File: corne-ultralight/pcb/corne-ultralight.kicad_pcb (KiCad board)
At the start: 2 copper layers, 275.5 x 105.6 mm, 136 parts, among them J2 OLED, J5 Breakaway_Tabs, J7 OLED, SW1 SW_PUSH, SW10 SW_PUSH, SW11 SW_PUSH, SW12 SW_PUSH, SW13 SW_PUSH, SW14 SW_PUSH, SW15 SW_PUSH, SW16 SW_PUSH, SW17 SW_PUSH, SW18 SW_PUSH, SW19 SW_PUSH, SW2 SW_PUSH, SW20 SW_PUSH, SW21 SW_PUSH, SW22 SW_PUSH, SW23 SW_PUSH, SW24 SW_PUSH, SW25 SW_PUSH, SW26 SW_PUSH, SW27 SW_PUSH, SW28 SW_PUSH, SW29 SW_PUSH, SW3 SW_PUSH, SW30 SW_PUSH, SW31 SW_PUSH, SW32 SW_PUSH, SW33 SW_PUSH, SW34 SW_PUSH, SW35 SW_PUSH, SW36 SW_PUSH, SW37 SW_PUSH, SW38 SW_PUSH, SW39 SW_PUSH, SW4 SW_PUSH, SW40 SW_PUSH, SW41 SW_PUSH, SW42 SW_PUSH, SW5 SW_PUSH, SW6 SW_PUSH, SW7 SW_PUSH, SW8 SW_PUSH, SW9 SW_PUSH, U1 ProMicro, U2 ProMicro

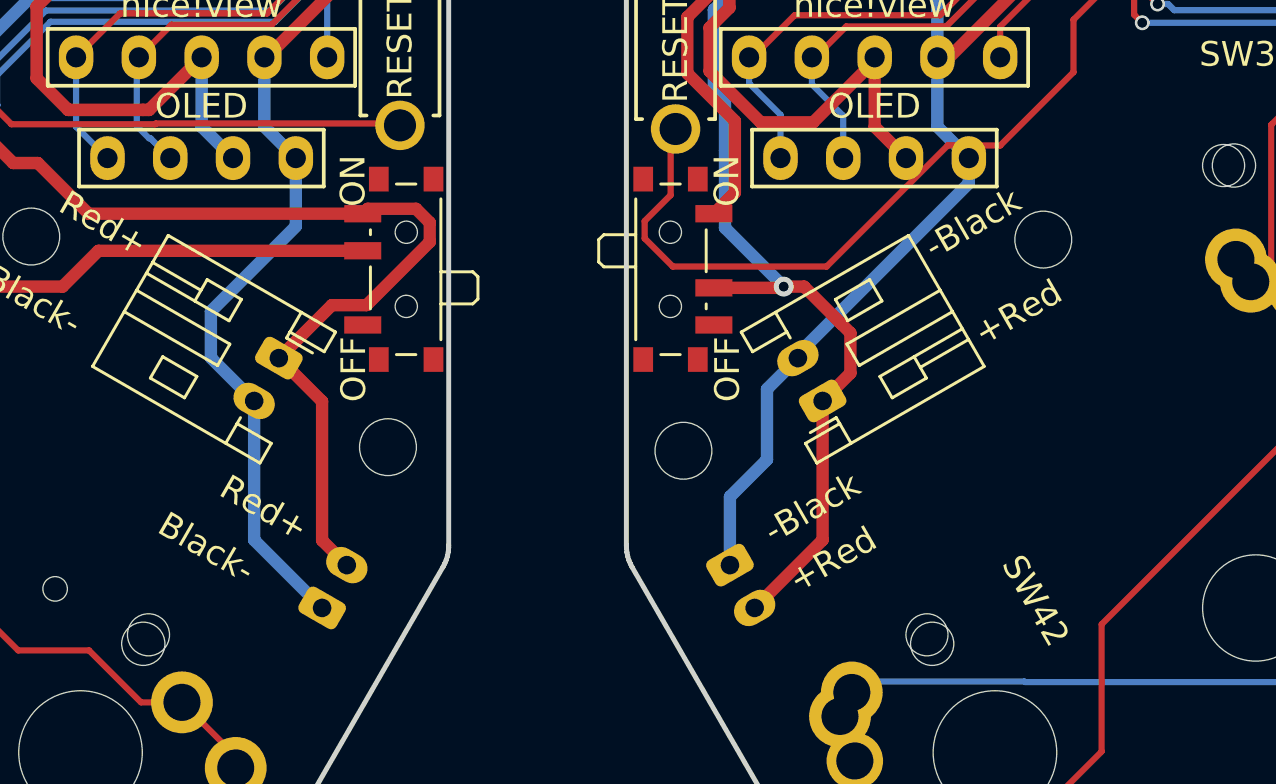
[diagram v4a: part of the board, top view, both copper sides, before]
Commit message: All JST connectors routed
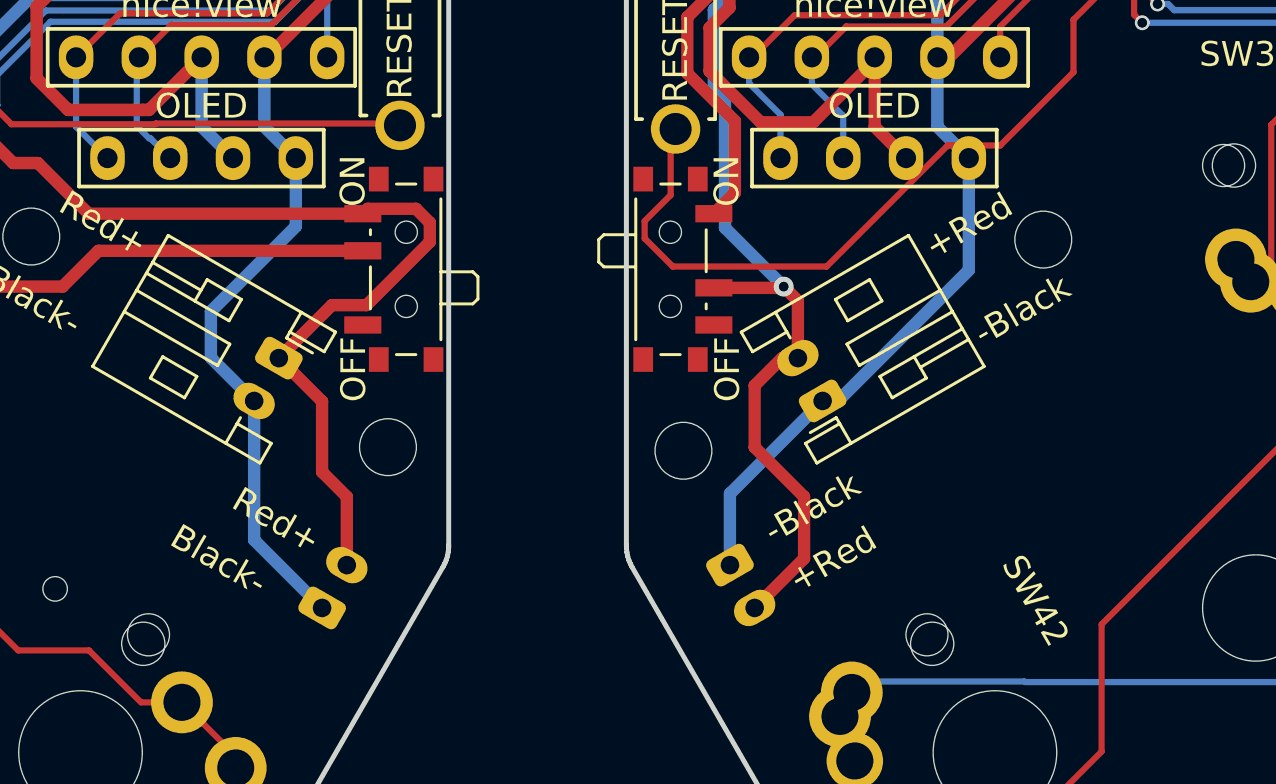
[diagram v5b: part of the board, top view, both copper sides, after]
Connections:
- BATJ5 pad 1: Net-(BATJ5-Pin_2) -> GNDA
- BATJ5 pad 2: GNDA -> Net-(BATJ5-Pin_2)
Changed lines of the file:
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@@
 			(remove_unused_layers no)
 			(roundrect_rratio 0.208333)
-			(net 18 "Net-(BATJ5-Pin_2)")
+			(net 38 "GNDA")
 			(pinfunction "Pin_1")
 			(pintype "passive")
@@
 			(layers "*.Cu" "*.Mask")
 			(remove_unused_layers no)
-			(net 38 "GNDA")
+			(net 18 "Net-(BATJ5-Pin_2)")
 			(pinfunction "Pin_2")
 			(pintype "passive")
@@
 	)
 	(gr_text "-Black"
-		(at 165.125347 79.445 90)
+		(at 166.7125 81.445 90)
 		(layer "B.SilkS")
 		(effects
@@
 	)
 	(gr_text "-Black"
-		(at 137.8625 79.445 90)
+		(at 138.2125 90.445 -30)
 		(layer "B.SilkS")
 		(effects
@@
 	)
 	(gr_text "-Black"
-		(locked yes)
-		(at 135.8375 95.945 -30)
+		(at 139.2125 80.945 90)
+		(layer "B.SilkS")
+		(effects
+			(font
+				(size 1 1)
+				(thickness 0.15)
+			)
+			(justify left mirror)
+		)
+	)
+	(gr_text "-Black"
+		(at 135.2125 96.945 -30)
 		(layer "B.SilkS")
 		(effects
@@
 	)
 	(gr_text "+Red"
-		(at 135.7375 79.445 90)
+		(at 134.2125 81.445 90)
+		(layer "B.SilkS")
+		(effects
+			(font
+				(size 1 1)
+				(thickness 0.15)
+			)
+			(justify left mirror)
+		)
+	)
+	(gr_text "Red+"
+		(at 165.7125 86.445 30)
 		(layer "B.SilkS")
 		(effects
@@
 	)
 	(gr_text "Black-"
-		(at 168.9625 91.195 30)
+		(at 168.2125 90.945 30)
 		(layer "B.SilkS")
 		(effects
@@
 	)
 	(gr_text "+Red"
-		(locked yes)
-		(at 136.7125 94.445 330)
+		(at 137.2125 93.945 330)
 		(layer "B.SilkS")
 		(effects
@@
 	)
 	(gr_text "+Red"
-		(at 163.000347 79.445 90)
+		(at 139.2125 88.445 330)
+		(layer "B.SilkS")
+		(effects
+			(font
+				(size 1 1)
+				(thickness 0.15)
+			)
+			(justify left mirror)
+		)
+	)
+	(gr_text "Black-"
+		(at 167.7125 87.945 30)
+		(layer "B.SilkS")
+		(effects
+			(font
+				(size 1 1)
+				(thickness 0.15)
+			)
+			(justify left mirror)
+		)
+	)
+	(gr_text "+Red"
+		(at 161.7125 81.445 90)
 		(layer "B.SilkS")
 		(effects
@@
 	)
 	(gr_text "Red+"
-		(at 168.9625 93.695 30)
+		(at 169.2125 94.445 30)
 		(layer "B.SilkS")
 		(effects
@@
 	)
 	(gr_text "-Black"
-		(at 166.2125 84.945 30)
+		(at 168.2125 88.445 30)
 		(layer "F.SilkS")
 		(effects
@@
 	)
 	(gr_text "Red+"
-		(at 137.7125 94.445 -30)
+		(at 138.2125 94.945 -30)
 		(layer "F.SilkS")
 		(effects
@@
 	)
 	(gr_text "+Red"
-		(at 168.2125 88.445 30)
+		(at 166.2125 84.945 30)
 		(layer "F.SilkS")
 		(effects
@@
 	)
 	(gr_text "Black-"
-		(at 135.2125 95.945 -30)
+		(at 135.7125 96.445 -30)
 		(layer "F.SilkS")
 		(effects
@@
 	)
 	(segment
+		(start 138.9625 91.07)
+		(end 138.9625 96.695)
+		(width 0.5)
+		(layer "B.Cu")
+		(net 5)
+	)
+	(segment
 		(start 139.3785 77.168)
 		(end 139.3785 79.975)
@@
 	)
 	(segment
+		(start 138.9625 96.695)
+		(end 141.7125 99.445)
+		(width 0.5)
+		(layer "B.Cu")
+		(net 5)
+	)
+	(segment
 		(start 127.5605 44.622)
 		(end 126.2625 45.92)
@@
 	)
 	(segment
-		(start 138.9625 96.695)
-		(end 141.7125 99.445)
-		(width 0.5)
-		(layer "B.Cu")
-		(net 5)
-	)
-	(segment
-		(start 138.9625 91.07)
-		(end 138.9625 96.695)
-		(width 0.5)
-		(layer "B.Cu")
-		(net 5)
-	)
-	(segment
 		(start 134.7115 79.295)
 		(end 136.8385 77.168)
@@
 	)
 	(segment
-		(start 141.7125 96.712949)
-		(end 142.7125 97.712949)
-		(width 0.5)
-		(layer "F.Cu")
-		(net 17)
-	)
-	(segment
 		(start 143.511003 87.195)
 		(end 142.105449 87.195)
@@
 	)
 	(segment
+		(start 141.7125 91.087949)
+		(end 141.7125 93.945)
+		(width 0.5)
+		(layer "F.Cu")
+		(net 17)
+	)
+	(segment
 		(start 146.0675 84.638503)
 		(end 143.511003 87.195)
@@
 	)
 	(segment
-		(start 141.7125 91.087949)
-		(end 141.7125 96.712949)
+		(start 145.511003 83.295)
+		(end 146.0675 83.851497)
 		(width 0.5)
 		(layer "F.Cu")
@@
 	)
 	(segment
-		(start 145.511003 83.295)
-		(end 146.0675 83.851497)
+		(start 143.5575 83.295)
+		(end 145.511003 83.295)
 		(width 0.5)
 		(layer "F.Cu")
@@
 	)
 	(segment
-		(start 143.5575 83.295)
-		(end 145.511003 83.295)
+		(start 141.7125 93.945)
+		(end 142.7125 94.945)
 		(width 0.5)
 		(layer "F.Cu")
@@
 	)
 	(segment
+		(start 142.7125 94.945)
+		(end 142.7125 97.712949)
+		(width 0.5)
+		(layer "F.Cu")
+		(net 17)
+	)
+	(segment
 		(start 143.3575 83.495)
 		(end 143.5575 83.295)
@@
 	)
 	(segment
-		(start 161.9625 96.695)
-		(end 161.9625 91.07)
+		(start 159.2125 90.445)
+		(end 159.2125 92.945)
 		(width 0.5)
 		(layer "F.Cu")
@@
 	)
 	(segment
-		(start 159.2125 99.445)
-		(end 161.9625 96.695)
+		(start 161.2125 97.445)
+		(end 161.2125 94.945)
 		(width 0.5)
 		(layer "F.Cu")
@@
 	)
 	(segment
-		(start 161.2125 86.445)
-		(end 162.7125 87.945)
+		(start 159.2125 92.945)
+		(end 161.2125 94.945)
 		(width 0.5)
 		(layer "F.Cu")
@@
 	)
 	(segment
-		(start 160.3875 86.445)
-		(end 161.2125 86.445)
+		(start 159.2125 99.445)
+		(end 161.2125 97.445)
+		(width 0.5)
+		(layer "F.Cu")
+		(net 18)
+	)
+	(segment
+		(start 160.9625 89.337949)
+		(end 160.319551 89.337949)
 		(width 0.5)
 		(layer "F.Cu")
@@
 	)
 	(segment
-		(start 163.0875 89.945)
-		(end 163.0875 88.32)
+		(start 160.9625 89.337949)
+		(end 160.9625 87.02)
 		(width 0.5)
 		(layer "F.Cu")
@@
 	)
 	(segment
-		(start 163.0875 89.945)
-		(end 161.9625 91.07)
+		(start 160.9625 87.02)
+		(end 160.3875 86.445)
 		(width 0.5)
 		(layer "F.Cu")
@@
 	)
 	(segment
-		(start 160.3875 86.445)
-		(end 160.3375 86.495)
+		(start 160.319551 89.337949)
+		(end 159.2125 90.445)
 		(width 0.5)
 		(layer "F.Cu")
@@
 	)
 	(segment
-		(start 163.0875 88.32)
-		(end 162.7125 87.945)
+		(start 160.3875 86.445)
+		(end 160.3375 86.495)
 		(width 0.5)
 		(layer "F.Cu")
@@
 	)
 	(segment
-		(start 160.9625 89.337949)
-		(end 160.819551 89.337949)
+		(start 161.9625 91.07)
+		(end 158.2125 94.82)
 		(width 0.5)
 		(layer "B.Cu")
@@
 	)
 	(segment
-		(start 160.9625 89.1775)
-		(end 167.8775 82.2625)
+		(start 166.6075 77.168)
+		(end 166.6075 79.975)
 		(width 0.5)
 		(layer "B.Cu")
@@
 	)
 	(segment
-		(start 166.6075 77.168)
-		(end 166.6075 79.975)
+		(start 162.5875 91.07)
+		(end 161.9625 91.07)
+		(width 0.5)
+		(layer "B.Cu")
+		(net 38)
+	)
+	(segment
+		(start 167.8775 85.78)
+		(end 162.5875 91.07)
 		(width 0.5)
 		(layer "B.Cu")
@@
 	)
 	(segment
-		(start 160.9625 89.337949)
-		(end 159.7125 90.587949)
+		(start 158.2125 94.82)
+		(end 158.2125 97.712949)
 		(width 0.5)
 		(layer "B.Cu")
@@
 	)
 	(segment
-		(start 160.9625 89.337949)
-		(end 160.9625 89.1775)
-		(width 0.5)
-		(layer "B.Cu")
-		(net 38)
-	)
-	(segment
 		(start 166.6075 77.31)
 		(end 166.6075 73.69)
@@
 	)
 	(segment
-		(start 159.7125 90.587949)
-		(end 159.7125 93.445)
-		(width 0.5)
-		(layer "B.Cu")
-		(net 38)
-	)
-	(segment
 		(start 156.374847 73.567432)
 		(end 159.047279 70.895)
@@
 	)
 	(segment
-		(start 166.6075 73.69)
-		(end 165.5125 72.595)
-		(width 0.5)
-		(layer "B.Cu")
-		(net 38)
-	)
-	(segment
-		(start 158.2125 94.945)
-		(end 158.2125 97.712949)
+		(start 167.8775 81.245)
+		(end 167.8775 85.78)
 		(width 0.5)
 		(layer "B.Cu")
@@
 	)
 	(segment
-		(start 167.8775 82.2625)
-		(end 167.8775 81.245)
-		(width 0.5)
-		(layer "B.Cu")
-		(net 38)
-	)
-	(segment
-		(start 159.7125 93.445)
-		(end 158.2125 94.945)
+		(start 166.6075 73.69)
+		(end 165.5125 72.595)
 		(width 0.5)
 		(layer "B.Cu")
@@
 	)
 	(group ""
-		(locked yes)
-		(members "4a996102-397b-4128-984c-9a8933ea2795" "c38c8af6-97b0-45ca-9a59-3da6802a5380")
-	)
-	(group ""
-		(members "1699eb40-3cd1-4b45-a255-a3766723f2aa" "a8656f61-20f2-4f4f-85e5-88240e3db9da")
-	)
-	(group ""
-		(members "bf2d9438-5707-45bb-afd9-16b03e8c02da" "f23a101d-0fbe-4204-b014-7e2938500171")
-	)
-	(group ""
-		(members "059fc2a2-ebc6-4b7c-8e8c-41927e56001a" "e7de1a86-f790-4754-ab25-9eb08d2c43eb")
-	)
-	(group ""
-		(members "76928853-158b-4ef6-8a75-f29738a21ab3" "f53d74c8-5604-44f4-925d-4a9276fe4176")
-	)
-	(group ""
 		(members "013f1f25-df12-4825-a242-8f30f3cd3b16" "5f772bcf-fc59-4ca1-a4e6-d1eedcd91c5c")
 	)
 	(group ""
-		(members "01479362-f1f3-4fd6-b3e6-c2a7d09f4203" "b6fb3f63-e80f-4c95-9414-9f3200ad5d20")
-	)
-	(group ""

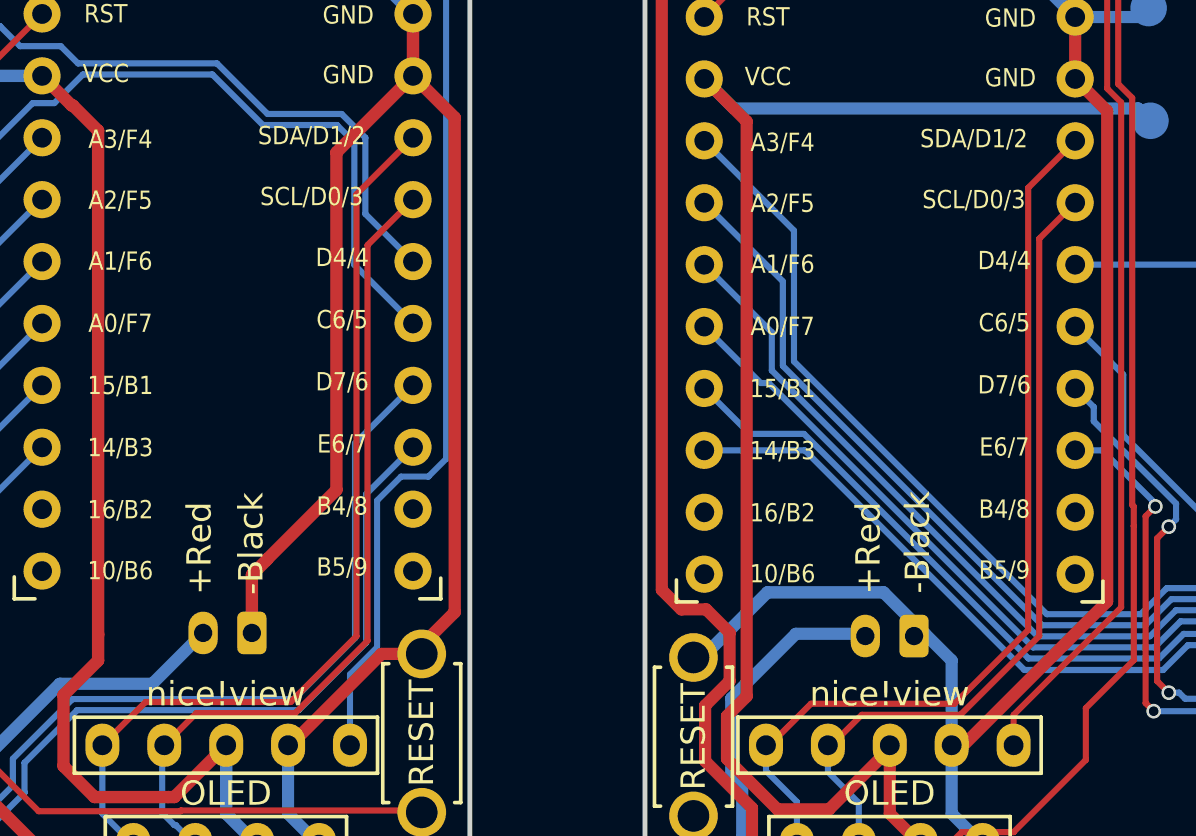
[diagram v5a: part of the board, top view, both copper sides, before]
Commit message: Middle JST moved below the MCU
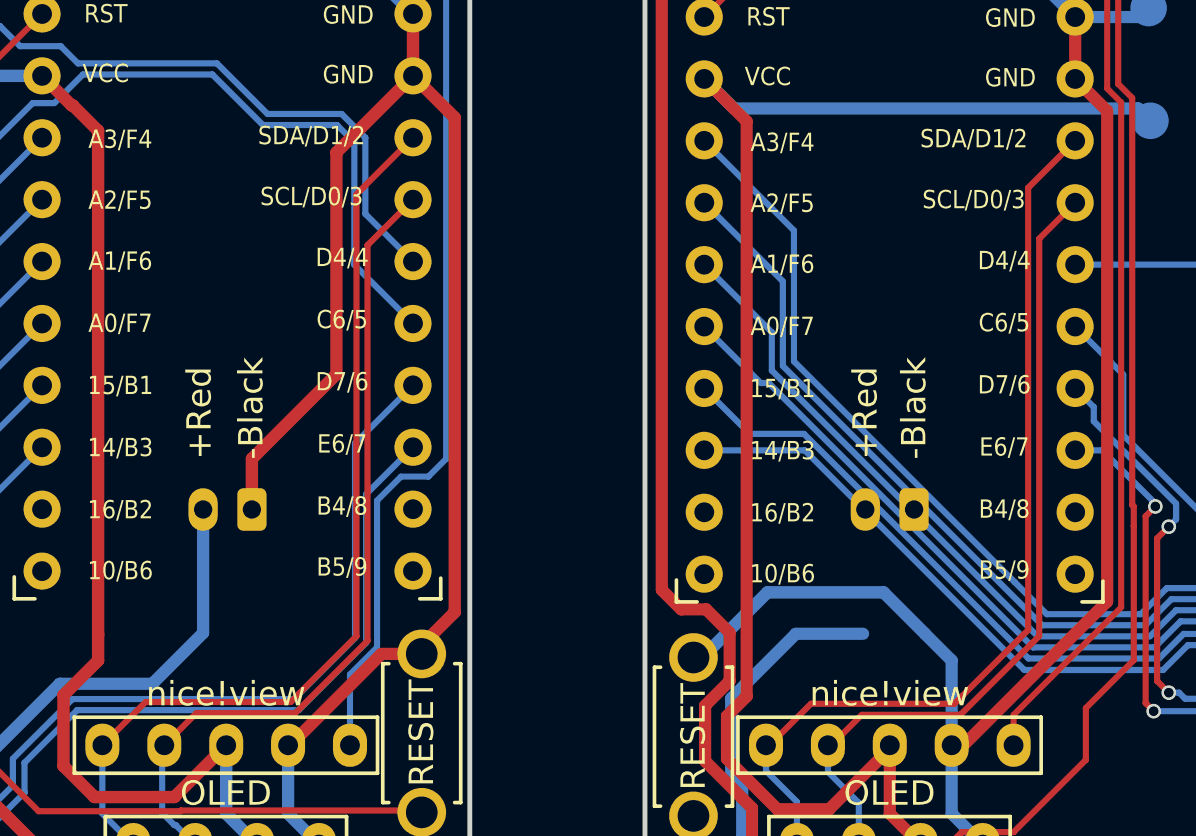
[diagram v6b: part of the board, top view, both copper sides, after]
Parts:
- moved BATJ4 5.19 mm to (165.1, 67.5)
- moved BATJ1 5.06 mm to (137.9, 67.5)
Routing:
- net Net-(BATJ1-Pin_2): track 52.1 -> 57.2 mm
- net GND: track 105.8 -> 100.7 mm
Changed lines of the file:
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@@
 	)
 	(footprint "Connector_JST:JST_PH_S2B-PH-K_1x02_P2.00mm_Horizontal"
-		(locked yes)
 		(layer "B.Cu")
-		(at 165.062847 72.686432 180)
+		(at 165.062847 67.495 180)
 		(descr "JST PH series connector, S2B-PH-K (http://www.jst-mfg.com/product/pdf/eng/ePH.pdf), generated with kicad-footprint-generator")
 		(tags "connector JST PH top entry")
@@
 	)
 	(footprint "Connector_JST:JST_PH_S2B-PH-K_1x02_P2.00mm_Horizontal"
-		(locked yes)
 		(layer "B.Cu")
-		(at 137.8925 72.56 180)
+		(at 137.8925 67.495 180)
 		(descr "JST PH series connector, S2B-PH-K (http://www.jst-mfg.com/product/pdf/eng/ePH.pdf), generated with kicad-footprint-generator")
 		(tags "connector JST PH top entry")
@@
 	)
 	(gr_text "-Black"
-		(at 166.7125 81.445 90)
+		(at 165.7125 63.945 -90)
 		(layer "B.SilkS")
 		(effects
@@
 	)
 	(gr_text "-Black"
-		(at 139.2125 80.945 90)
+		(at 135.2125 96.945 -30)
 		(layer "B.SilkS")
 		(effects
@@
 		)
 	)
-	(gr_text "-Black"
-		(at 135.2125 96.945 -30)
+	(gr_text "+Red"
+		(at 135.2125 63.945 -90)
 		(layer "B.SilkS")
 		(effects
@@
 		)
 	)
-	(gr_text "+Red"
-		(at 134.2125 81.445 90)
+	(gr_text "-Black"
+		(at 138.7125 63.945 -90)
 		(layer "B.SilkS")
 		(effects
@@
 	)
 	(gr_text "+Red"
-		(at 161.7125 81.445 90)
+		(at 162.2125 63.945 -90)
 		(layer "B.SilkS")
 		(effects
@@
 	)
 	(gr_text "+Red"
-		(at 135.7375 70.995 90)
+		(at 135.7375 65.445 90)
 		(layer "F.SilkS")
 		(effects
@@
 	)
 	(gr_text "+Red"
-		(at 163.1875 70.995 90)
+		(at 163.062847 65.445 90)
 		(layer "F.SilkS")
 		(effects
@@
 	)
 	(gr_text "-Black"
-		(at 165.2125 70.945 90)
+		(at 165.062847 65.445 90)
 		(layer "F.SilkS")
 		(effects
@@
 	)
 	(gr_text "-Black"
-		(at 137.8625 70.995 90)
+		(at 137.8625 65.445 90)
 		(layer "F.SilkS")
 		(effects
@@
 	)
 	(segment
-		(start 141.3625 52.8434)
-		(end 141.3625 66.695)
-		(width 0.508)
-		(layer "F.Cu")
-		(net 5)
-	)
-	(segment
-		(start 137.8925 70.175)
-		(end 137.8925 72.56)
-		(width 0.508)
-		(layer "F.Cu")
-		(net 5)
-	)
-	(segment
-		(start 141.3625 66.695)
-		(end 138.5225 69.535)
+		(start 137.8925 65.415)
+		(end 141.3625 61.945)
 		(width 0.508)
 		(layer "F.Cu")
@@
 	)
 	(segment
+		(start 141.3625 52.8434)
+		(end 141.3625 61.945)
+		(width 0.508)
+		(layer "F.Cu")
+		(net 5)
+	)
+	(segment
 		(start 144.5045 73.421)
 		(end 146.2145 71.711)
@@
 	)
 	(segment
-		(start 138.5225 69.545)
-		(end 137.8925 70.175)
-		(width 0.508)
-		(layer "F.Cu")
-		(net 5)
-	)
-	(segment
-		(start 138.5225 69.535)
-		(end 138.5225 69.545)
+		(start 137.8925 67.495)
+		(end 137.8925 65.415)
 		(width 0.508)
 		(layer "F.Cu")
@@
 	)
 	(segment
-		(start 130.0125 74.645)
-		(end 133.8075 74.645)
+		(start 135.8925 72.56)
+		(end 135.8925 67.495)
 		(width 0.5)
 		(layer "B.Cu")
@@
 	)
 	(segment
-		(start 126.9125 77.745)
-		(end 130.0125 74.645)
+		(start 130.0125 74.645)
+		(end 133.8075 74.645)
 		(width 0.5)
 		(layer "B.Cu")
@@
 	(segment
 		(start 133.8075 74.645)
-		(end 135.8575 72.595)
+		(end 135.8925 72.56)
+		(width 0.5)
+		(layer "B.Cu")
+		(net 17)
+	)
+	(segment
+		(start 126.9125 77.745)
+		(end 130.0125 74.645)
 		(width 0.5)
 		(layer "B.Cu")
@@
 	)
 	(segment
-		(start 236.613739 68.634392)
-		(end 236.63379 68.654443)
+		(start 169.1875 70.47)
+		(end 170.507877 71.790377)
 		(width 0.254)
 		(layer "B.Cu")
@@
 	)
 	(segment
-		(start 253.464847 67.110432)
-		(end 256.786558 67.110432)
+		(start 160.134847 61.417347)
+		(end 169.1875 70.47)
 		(width 0.254)
 		(layer "B.Cu")
@@
 	)
 	(segment
-		(start 160.134847 61.417347)
-		(end 170.507877 71.790377)
+		(start 236.613739 68.634392)
+		(end 236.63379 68.654443)
+		(width 0.254)
+		(layer "B.Cu")
+		(net 26)
+	)
+	(segment
+		(start 253.464847 67.110432)
+		(end 256.786558 67.110432)
 		(width 0.254)
 		(layer "B.Cu")
